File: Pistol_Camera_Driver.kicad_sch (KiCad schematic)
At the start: 67 parts, among them J1 Screw_Terminal_01x02, J10 Screw_Terminal_01x02, J11 Screw_Terminal_01x02, J12 I2C, J13 Screw_Terminal_01x02, J14 Bluetooth, J15 I2C, J16 I2C, J2 Screw_Terminal_01x02, J3 Objective, J4 Screw_Terminal_01x02, J5 Joystick, J6 Screw_Terminal_01x02, J7 Screw_Terminal_01x02, J8 Screw_Terminal_01x02, J9 I2C, K1 IM03, M1 Fan, Q1 FFB2222A, Q2 AO3400A, U1 LM7805_TO220, U2 LM317_TO-263, U3 Raspberri_Pi_Pico, U4 DRV8834PWP, U5 DRV8834PWP, U6 RS0101YH6, U7 LDD-700L

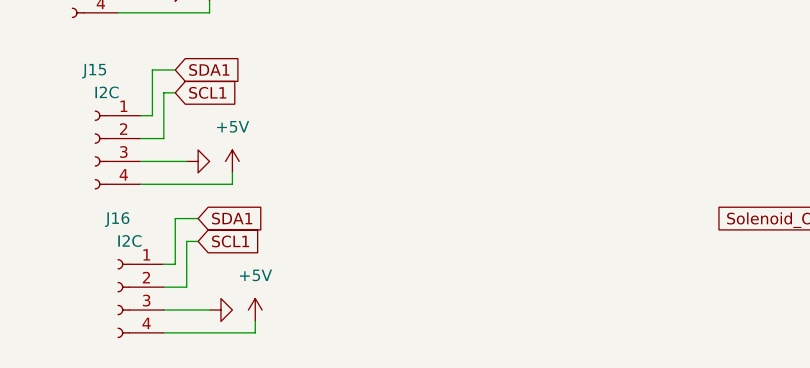
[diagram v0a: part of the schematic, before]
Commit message: v0.4 5th I2C connector was added. Seems 2B ready.
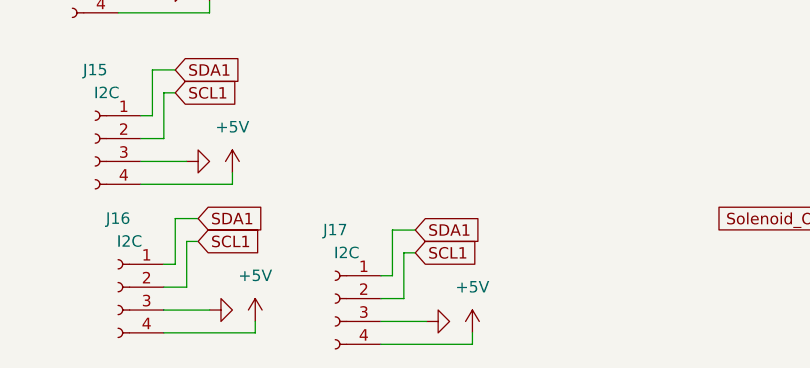
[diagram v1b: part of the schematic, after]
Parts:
- added J17: I2C, Connector_PinSocket_2.54mm:PinSocket_1x04_P2.54mm_Vertical, symbol Connector:Conn_01x04_Female
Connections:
- net +5V: now also J17.4 (Pin_4)
- net GND: now also J17.3 (Pin_3)
- net SCL1: now also J17.2 (Pin_2)
- net SDA1: now also J17.1 (Pin_1)
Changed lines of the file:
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@@
     (stroke (width 0) (type default) (color 0 0 0 0))
   )
+  (wire (pts (xy 72.39 184.15) (xy 73.66 184.15))
+    (stroke (width 0) (type default) (color 0 0 0 0))
+  )
   (wire (pts (xy 64.77 100.33) (xy 64.77 95.25))
     (stroke (width 0) (type default) (color 0 0 0 0))
@@
     (stroke (width 0) (type default) (color 0 0 0 0))
   )
+  (wire (pts (xy 69.85 189.23) (xy 72.39 189.23))
+    (stroke (width 0) (type default) (color 0 0 0 0))
+  )
   (wire (pts (xy 144.78 151.13) (xy 144.78 156.21))
     (stroke (width 0) (type default) (color 0 0 0 0))
@@
     (stroke (width 0) (type default) (color 0 0 0 0))
   )
+  (wire (pts (xy 69.85 194.31) (xy 80.01 194.31))
+    (stroke (width 0) (type default) (color 0 0 0 0))
+  )
   (wire (pts (xy 247.65 49.53) (xy 248.92 49.53))
     (stroke (width 0) (type default) (color 0 0 0 0))
@@
     (stroke (width 0) (type default) (color 0 0 0 0))
   )
+  (wire (pts (xy 69.85 191.77) (xy 74.93 191.77))
+    (stroke (width 0) (type default) (color 0 0 0 0))
+  )
   (wire (pts (xy 274.32 40.64) (xy 275.59 40.64))
     (stroke (width 0) (type default) (color 0 0 0 0))
@@
     (stroke (width 0) (type default) (color 0 0 0 0))
   )
+  (wire (pts (xy 80.01 193.04) (xy 80.01 194.31))
+    (stroke (width 0) (type default) (color 0 0 0 0))
+  )
   (wire (pts (xy 276.86 91.44) (xy 276.86 93.98))
     (stroke (width 0) (type default) (color 0 0 0 0))
@@
     (stroke (width 0) (type default) (color 0 0 0 0))
   )
+  (wire (pts (xy 69.85 186.69) (xy 71.12 186.69))
+    (stroke (width 0) (type default) (color 0 0 0 0))
+  )
   (wire (pts (xy 45.72 187.96) (xy 48.26 187.96))
     (stroke (width 0) (type default) (color 0 0 0 0))
@@
     (stroke (width 0) (type default) (color 0 0 0 0))
   )
+  (wire (pts (xy 72.39 189.23) (xy 72.39 184.15))
+    (stroke (width 0) (type default) (color 0 0 0 0))
+  )
   (wire (pts (xy 81.28 44.45) (xy 81.28 45.72))
     (stroke (width 0) (type default) (color 0 0 0 0))
@@
     (stroke (width 0) (type default) (color 0 0 0 0))
   )
+  (wire (pts (xy 71.12 181.61) (xy 71.12 186.69))
+    (stroke (width 0) (type default) (color 0 0 0 0))
+  )
   (wire (pts (xy 265.43 78.74) (xy 265.43 82.55))
     (stroke (width 0) (type default) (color 0 0 0 0))
@@
     (stroke (width 0) (type default) (color 0 0 0 0))
   )
+  (wire (pts (xy 73.66 181.61) (xy 71.12 181.61))
+    (stroke (width 0) (type default) (color 0 0 0 0))
+  )
   (wire (pts (xy 123.19 19.05) (xy 123.19 16.51))
     (stroke (width 0) (type default) (color 0 0 0 0))
@@
     )
   )
+  (global_label "SCL1" (shape input) (at 73.66 184.15 0) (fields_autoplaced)
+    (effects (font (size 1.27 1.27)) (justify left))
+    (property "Intersheet References" "${INTERSHEET_REFS}" (id 0) (at 80.7902 184.0706 0)
+      (effects (font (size 1.27 1.27)) (justify left) hide)
+    )
+  )
   (global_label "nFLT2" (shape input) (at 261.62 107.95 0) (fields_autoplaced)
     (effects (font (size 1.27 1.27)) (justify left))
@@
     )
   )
+  (global_label "SDA1" (shape input) (at 73.66 181.61 0) (fields_autoplaced)
+    (effects (font (size 1.27 1.27)) (justify left))
+    (property "Intersheet References" "${INTERSHEET_REFS}" (id 0) (at 80.8507 181.5306 0)
+      (effects (font (size 1.27 1.27)) (justify left) hide)
+    )
+  )
   (global_label "AOUT2_1" (shape input) (at 274.32 33.02 180) (fields_autoplaced)
     (effects (font (size 1.27 1.27)) (justify right))
@@
     (pin "1")
   )
+  (symbol (lib_id "Connector:Conn_01x04_Female") (at 64.77 189.23 0) (mirror y) (unit 1)
+    (in_bom yes) (on_board yes)
+    (property "Reference" "J17" (id 0) (at 64.77 181.61 0))
+    (property "Value" "I2C" (id 1) (at 66.04 184.15 0))
+    (property "Footprint" "Connector_PinSocket_2.54mm:PinSocket_1x04_P2.54mm_Vertical" (id 2) (at 64.77 189.23 0)
+      (effects (font (size 1.27 1.27)) hide)
+    )
+    (property "Datasheet" "~" (id 3) (at 64.77 189.23 0)
+      (effects (font (size 1.27 1.27)) hide)
+    )
+    (pin "1")
+    (pin "2")
+    (pin "3")
+    (pin "4")
+  )
   (symbol (lib_id "Device:R") (at 181.61 134.62 270) (mirror x) (unit 1)
     (in_bom yes) (on_board yes) (fields_autoplaced)
@@
     (pin "1")
   )
+  (symbol (lib_id "power:+5V") (at 80.01 193.04 0) (unit 1)
+    (in_bom yes) (on_board yes) (fields_autoplaced)
+    (property "Reference" "#PWR071" (id 0) (at 80.01 196.85 0)
+      (effects (font (size 1.27 1.27)) hide)
+    )
+    (property "Value" "+5V" (id 1) (at 80.01 187.96 0))
+    (property "Footprint" "" (id 2) (at 80.01 193.04 0)
+      (effects (font (size 1.27 1.27)) hide)
+    )
+    (property "Datasheet" "" (id 3) (at 80.01 193.04 0)
+      (effects (font (size 1.27 1.27)) hide)
+    )
+    (pin "1")
+  )
   (symbol (lib_id "Connector:Conn_01x05_Female") (at 59.69 59.69 0) (mirror y) (unit 1)
     (in_bom yes) (on_board yes) (fields_autoplaced)
@@
     (pin "2")
   )
+  (symbol (lib_id "power:GND") (at 74.93 191.77 90) (unit 1)
+    (in_bom yes) (on_board yes) (fields_autoplaced)
+    (property "Reference" "#PWR070" (id 0) (at 81.28 191.77 0)
+      (effects (font (size 1.27 1.27)) hide)
+    )
+    (property "Value" "GND" (id 1) (at 80.01 191.77 0)
+      (effects (font (size 1.27 1.27)) hide)
+    )
+    (property "Footprint" "" (id 2) (at 74.93 191.77 0)
+      (effects (font (size 1.27 1.27)) hide)
+    )
+    (property "Datasheet" "" (id 3) (at 74.93 191.77 0)
+      (effects (font (size 1.27 1.27)) hide)
+    )
+    (pin "1")
+  )
   (symbol (lib_id "Connector:Screw_Terminal_01x02") (at 118.11 133.35 0) (unit 1)
     (in_bom yes) (on_board yes) (fields_autoplaced)
@@
       (reference "#PWR069") (unit 1) (value "+5V") (footprint "")
     )
+    (path "/e0423aae-62f6-458e-bfc3-807f66691924"
+      (reference "#PWR070") (unit 1) (value "GND") (footprint "")
+    )
+    (path "/8f2e72d0-4fb4-4f40-b38f-a9a606ff8d3c"
+      (reference "#PWR071") (unit 1) (value "+5V") (footprint "")
+    )
     (path "/f4a2552d-24c0-4848-8ca8-7dca516fd278"
       (reference "C1") (unit 1) (value "0.33") (footprint "Capacitor_SMD:C_0603_1608Metric_Pad1.08x0.95mm_HandSolder")
@@
       (reference "J16") (unit 1) (value "I2C") (footprint "Connector_PinSocket_2.54mm:PinSocket_1x04_P2.54mm_Vertical")
     )
+    (path "/309d5684-dc7c-4967-8535-170de839af9c"
+      (reference "J17") (unit 1) (value "I2C") (footprint "Connector_PinSocket_2.54mm:PinSocket_1x04_P2.54mm_Vertical")
+    )
     (path "/5115d19b-8d11-49ce-b309-80dd053f468d"

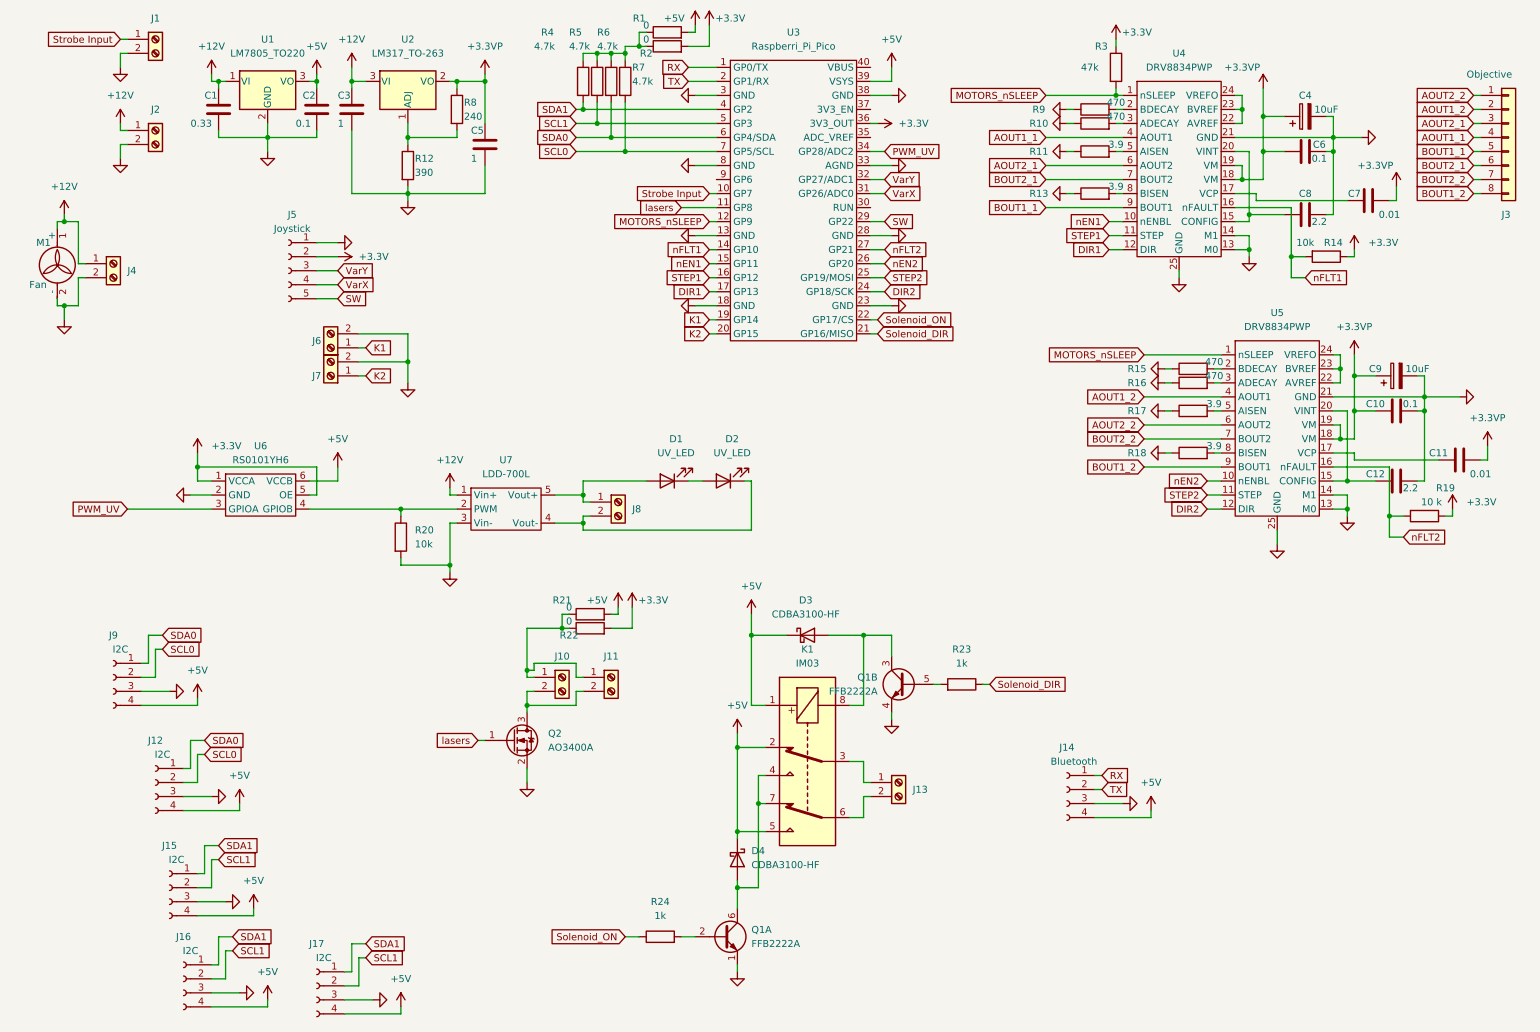
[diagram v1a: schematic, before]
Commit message: v0.5 I2C multiplexer, 5 I2C cnnectors, dirty routing
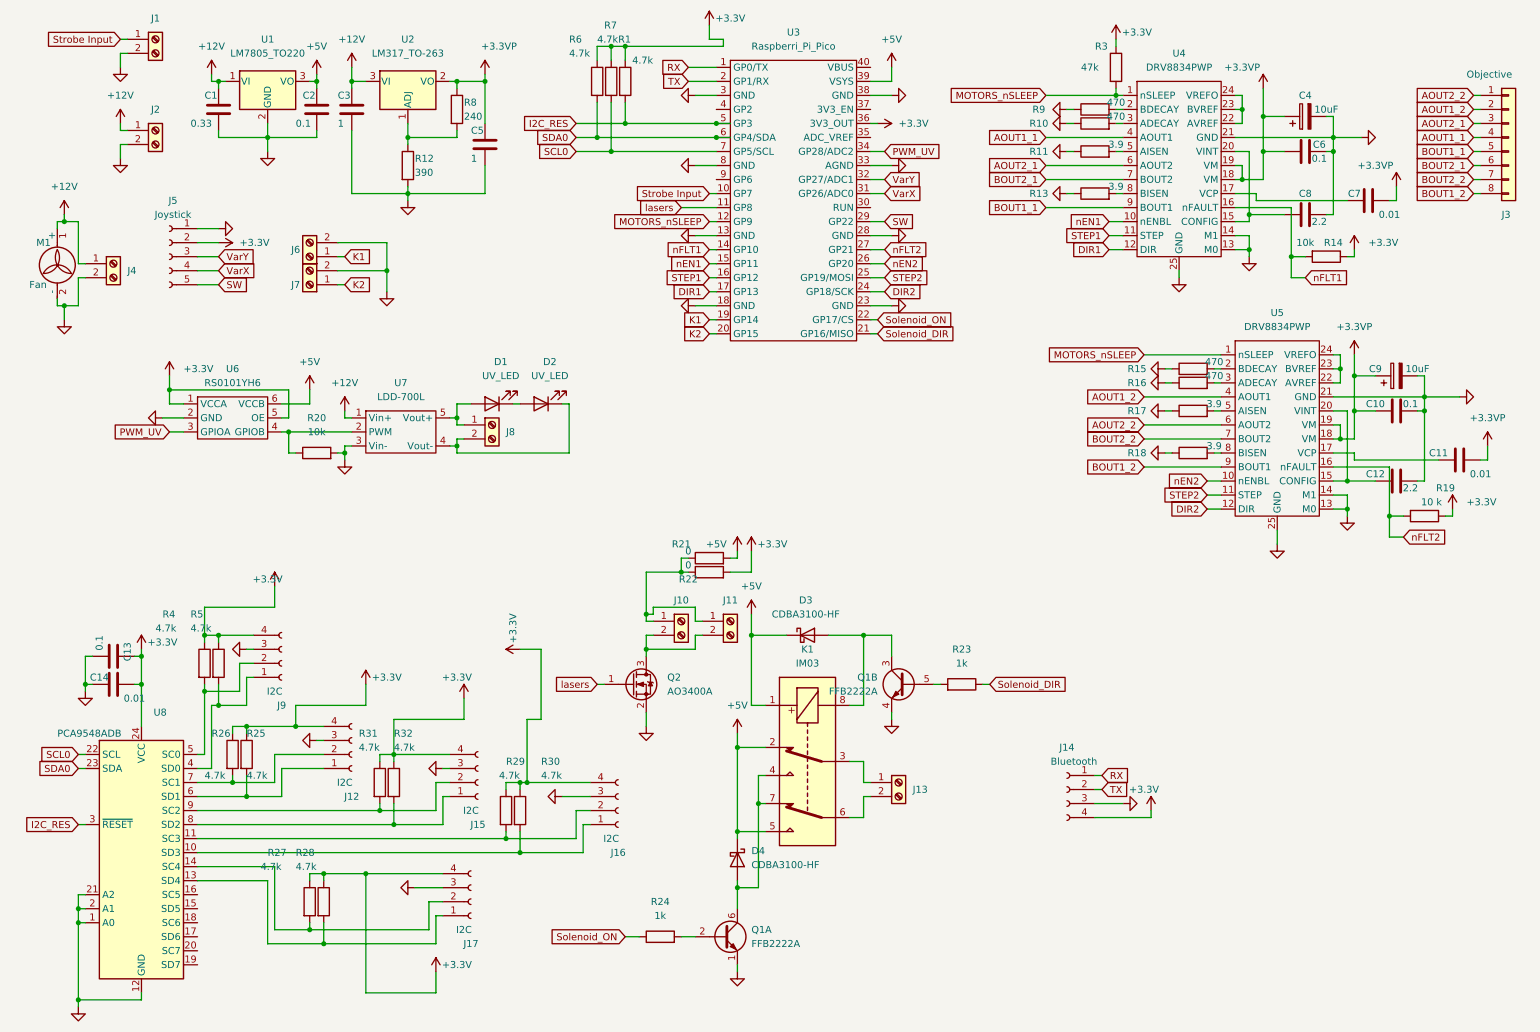
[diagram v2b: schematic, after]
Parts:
- removed R2: 0, Resistor_SMD:R_0603_1608Metric_Pad0.98x0.95mm_HandSolder, symbol Device:R
- added C13: 0.1, Capacitor_SMD:C_0603_1608Metric_Pad1.08x0.95mm_HandSolder, symbol Device:C
- added C14: 0.01, Capacitor_SMD:C_0603_1608Metric_Pad1.08x0.95mm_HandSolder, symbol Device:C
- added R25, R26, R27, R28, R29, R30, R31, R32: 4.7k, Resistor_SMD:R_0603_1608Metric_Pad0.98x0.95mm_HandSolder, symbol Device:R
- added U8: PCA9548ADB, Package_SO:SSOP-24_5.3x8.2mm_P0.65mm, symbol Interface_Expansion:PCA9548ADB
- R1: value 0 -> 4.7k
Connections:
- net +3V3: now also J12.4 (Pin_4), J14.4 (Pin_4), J15.4 (Pin_4), J16.4 (Pin_4), J17.4 (Pin_4), J9.4 (Pin_4), R1.1, R4.1, R5.1, R6.1, R7.1, C13.1, C14.2, R25.1, R26.1, R27.1, R28.1, R29.1, R30.1, R31.1, R32.1, U8.24 (VCC)
- net +5V: no longer J12.4 (Pin_4), J14.4 (Pin_4), J15.4 (Pin_4), J16.4 (Pin_4), J17.4 (Pin_4), J9.4 (Pin_4), R1.2
- net GND: now also C13.2, C14.1, U8.1 (A0), U8.12 (GND), U8.2 (A1), U8.21 (A2)
- net SCL0: now also U8.22 (SCL); no longer J12.2 (Pin_2), J9.2 (Pin_2)
- net SDA0: now also U8.23 (SDA); no longer J12.1 (Pin_1), J9.1 (Pin_1)
- removed net SCL1: J15.2 (Pin_2), J16.2 (Pin_2), J17.2 (Pin_2), R5.2, U3.5 (GP3)
- removed net SDA1: J15.1 (Pin_1), J16.1 (Pin_1), J17.1 (Pin_1), R4.2, U3.4 (GP2)
- new net: J16.2 (Pin_2), R29.2, U8.11 (SC3)
- new net: J17.1 (Pin_1), R28.2, U8.13 (SD4)
- new net: J16.1 (Pin_1), R30.2, U8.10 (SD3)
- new net: J17.2 (Pin_2), R27.2, U8.14 (SC4)
- new net: J9.1 (Pin_1), R5.2, U8.4 (SD0)
- new net: J9.2 (Pin_2), R4.2, U8.5 (SC0)
- new net: J12.1 (Pin_1), R26.2, U8.6 (SD1)
- new net: J12.2 (Pin_2), R25.2, U8.7 (SC1)
- new net: J15.1 (Pin_1), R32.2, U8.8 (SD2)
- new net: J15.2 (Pin_2), R31.2, U8.9 (SC2)
- new net I2C_RES: R1.2, U3.5 (GP3), U8.3 (~{RESET})
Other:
- moved on the sheet: D1, D2, J10, J11, J12, J15, J16, J17, J5, J6, J7, J8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

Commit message: v0.6 thermal sensors, led strips, i2c Multiplexer were added. Ordered!
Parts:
- removed J6, J7: Screw_Terminal_01x02, Connector_PinSocket_2.54mm:PinSocket_1x02_P2.54mm_Vertical, symbol Connector:Screw_Terminal_01x02
- added J6, J7: Conn_01x03_Socket, Connector_PinSocket_2.54mm:PinSocket_1x03_P2.54mm_Vertical, symbol Connector:Conn_01x03_Socket
- added R2: 4k7, Resistor_SMD:R_0603_1608Metric_Pad0.98x0.95mm_HandSolder, symbol Device:R
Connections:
- net GND: now also J6.3 (Pin_3), J7.3 (Pin_3)
- net V_lasers: now reaches J10.1 (Pin_1), J11.1 (Pin_1), R21.1, R22.1
- net V_lasers: now also J6.1 (Pin_1), J7.1 (Pin_1), R2.1
- net K1: no longer names the net of U3.19 (GP14)
- net K2 renamed Thermo
- net Thermo: now also J6.2 (Pin_2), J7.2 (Pin_2), R2.2
